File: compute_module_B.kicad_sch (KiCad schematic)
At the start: 2 parts

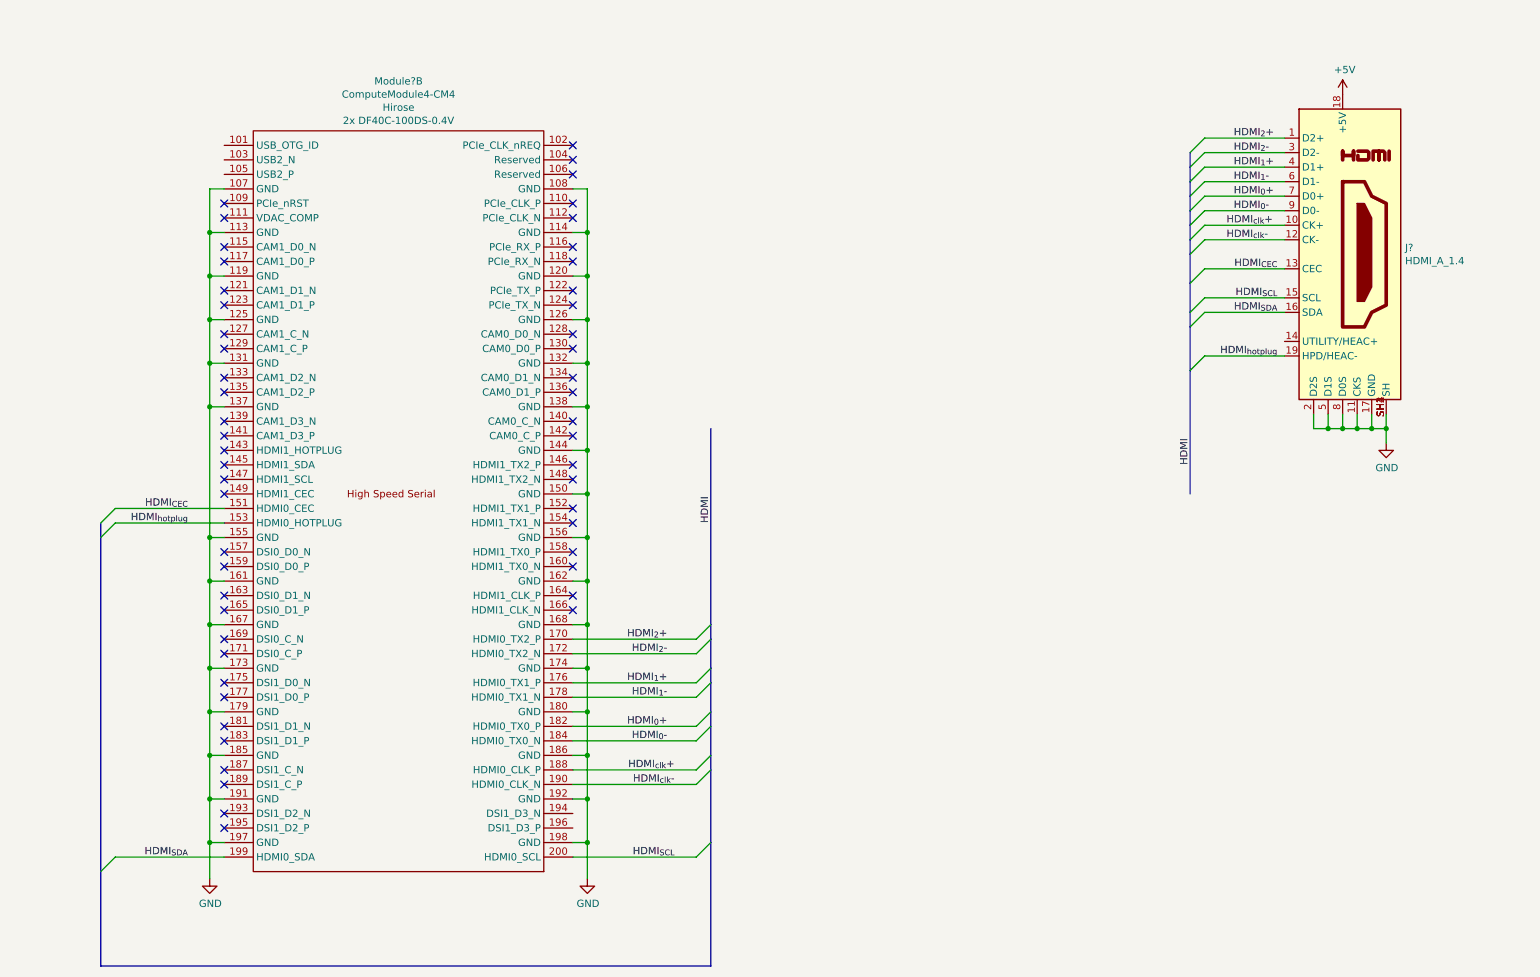
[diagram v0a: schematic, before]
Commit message: Added USB hub IC
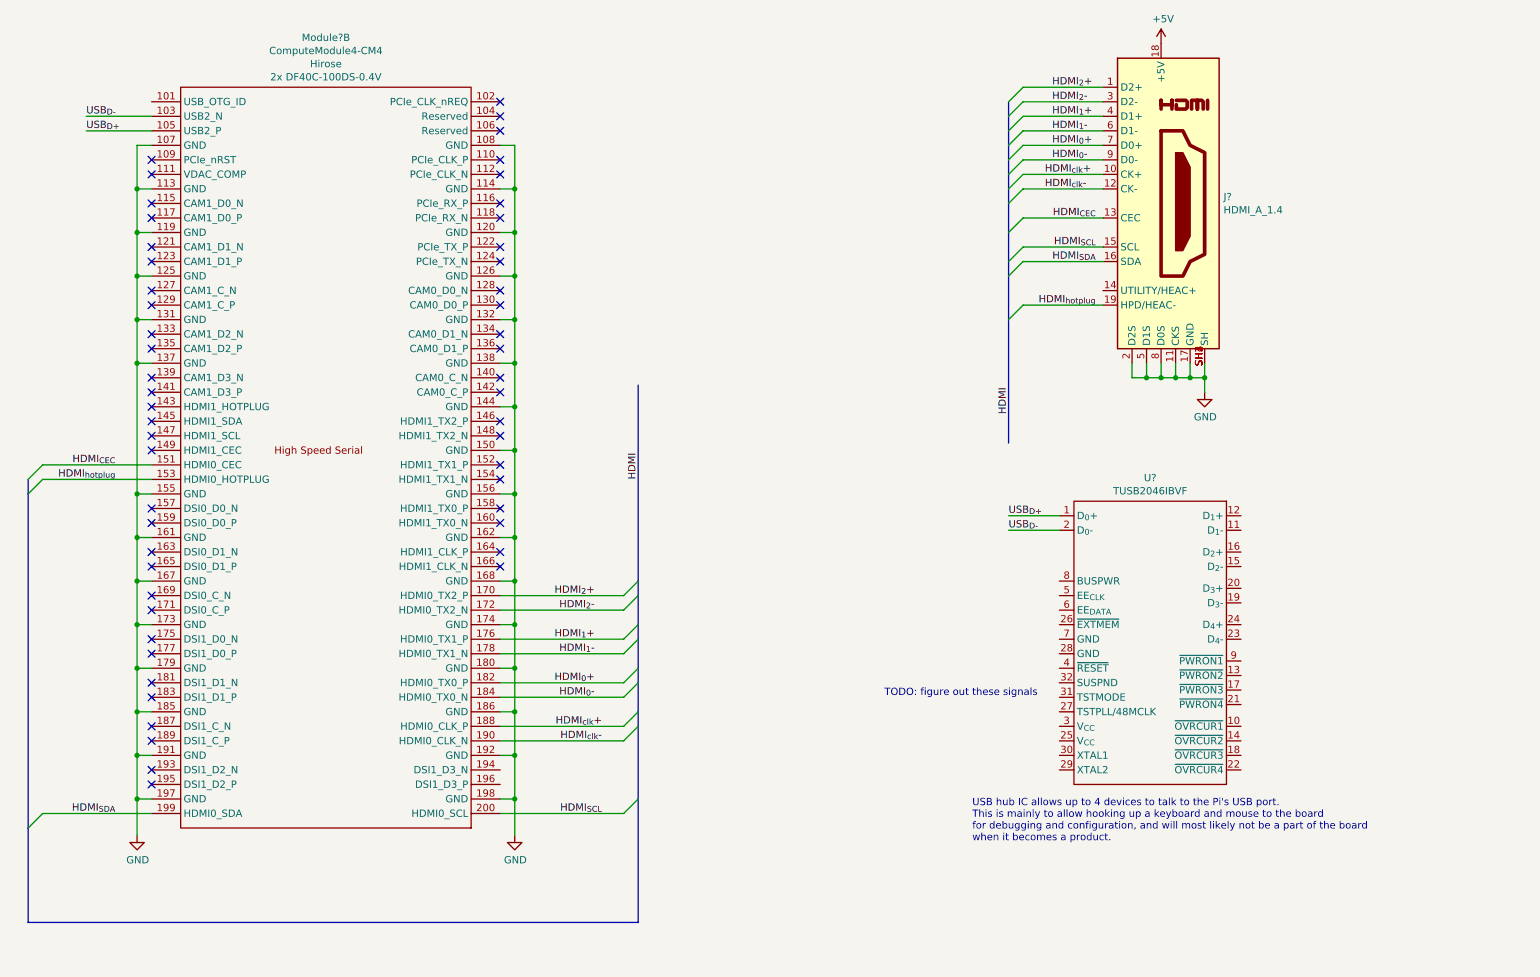
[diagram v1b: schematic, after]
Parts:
- added U?: TUSB2046IBVF, Package_QFP:LQFP-32_7x7mm_P0.8mm, symbol symbols:TUSB2046IBVF
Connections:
- net USB_{D-}: now reaches Module?.103 (USB2_N)
- net USB_{D-}: now also U?.2 (D_{0}-)
- net USB_{D+}: now reaches Module?.105 (USB2_P)
- net USB_{D+}: now also U?.1 (D_{0}+)
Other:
- note added: "TODO: figure out these signals"
- note added: "USB hub IC allows up to 4 devices to talk to the Pi's USB port. This is mainly to allow hooking up a keyboard and mouse to the board for debugging and configuration, and will most likely not be a part of the board when it becomes a product."
- moved on the sheet: J?, Module?B
